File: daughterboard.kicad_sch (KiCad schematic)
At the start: 1 part, among them J1 Programming

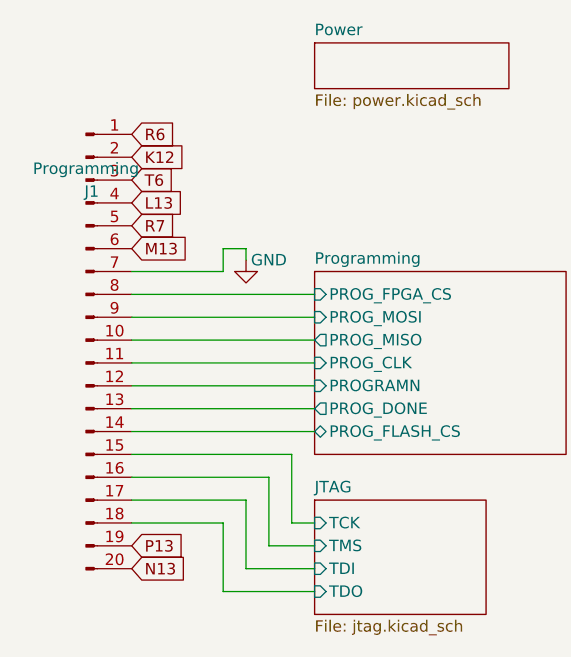
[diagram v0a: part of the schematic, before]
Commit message: Small routing tweaks, add breakout to schematic
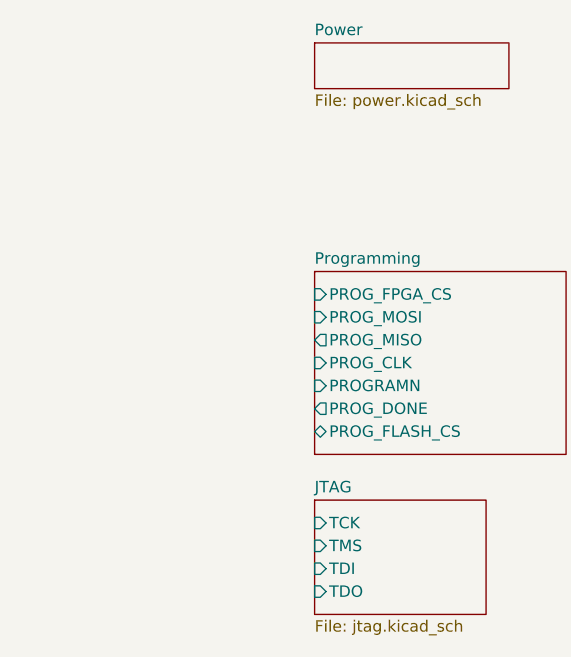
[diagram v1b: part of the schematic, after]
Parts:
- removed J1: Programming, Connector_PinHeader_2.54mm:PinHeader_2x10_P2.54mm_Vertical, symbol Connector:Conn_01x20_Pin
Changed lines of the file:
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@@
 (kicad_sch (version 20230121) (generator eeschema)
   (paper "A4")
-  (wire (pts (xy 123.19 104.14) (xy 118.11 104.14))
-    (stroke (width 0) (type default))
-  )
-  (wire (pts (xy 102.87 91.44) (xy 123.19 91.44))
-    (stroke (width 0) (type default))
-  )
-  (wire (pts (xy 113.03 71.12) (xy 113.03 73.66))
-    (stroke (width 0) (type default))
-  )
-  (wire (pts (xy 102.87 81.28) (xy 123.19 81.28))
-    (stroke (width 0) (type default))
-  )
-  (wire (pts (xy 102.87 101.6) (xy 113.03 101.6))
-    (stroke (width 0) (type default))
-  )
-  (wire (pts (xy 113.03 109.22) (xy 113.03 101.6))
-    (stroke (width 0) (type default))
-  )
-  (wire (pts (xy 120.65 93.98) (xy 120.65 101.6))
-    (stroke (width 0) (type default))
-  )
-  (wire (pts (xy 102.87 93.98) (xy 120.65 93.98))
-    (stroke (width 0) (type default))
-  )
-  (wire (pts (xy 123.19 106.68) (xy 115.57 106.68))
-    (stroke (width 0) (type default))
-  )
-  (wire (pts (xy 115.57 106.68) (xy 115.57 99.06))
-    (stroke (width 0) (type default))
-  )
-  (wire (pts (xy 115.57 71.12) (xy 113.03 71.12))
-    (stroke (width 0) (type default))
-  )
-  (wire (pts (xy 123.19 109.22) (xy 113.03 109.22))
-    (stroke (width 0) (type default))
-  )
-  (wire (pts (xy 102.87 96.52) (xy 118.11 96.52))
-    (stroke (width 0) (type default))
-  )
-  (wire (pts (xy 102.87 78.74) (xy 123.19 78.74))
-    (stroke (width 0) (type default))
-  )
-  (wire (pts (xy 102.87 88.9) (xy 123.19 88.9))
-    (stroke (width 0) (type default))
-  )
-  (wire (pts (xy 118.11 104.14) (xy 118.11 96.52))
-    (stroke (width 0) (type default))
-  )
-  (wire (pts (xy 115.57 72.39) (xy 115.57 71.12))
-    (stroke (width 0) (type default))
-  )
-  (wire (pts (xy 102.87 76.2) (xy 123.19 76.2))
-    (stroke (width 0) (type default))
-  )
-  (wire (pts (xy 102.87 83.82) (xy 123.19 83.82))
-    (stroke (width 0) (type default))
-  )
-  (wire (pts (xy 120.65 101.6) (xy 123.19 101.6))
-    (stroke (width 0) (type default))
-  )
-  (wire (pts (xy 102.87 99.06) (xy 115.57 99.06))
-    (stroke (width 0) (type default))
-  )
-  (wire (pts (xy 102.87 73.66) (xy 113.03 73.66))
-    (stroke (width 0) (type default))
-  )
-  (wire (pts (xy 102.87 86.36) (xy 123.19 86.36))
-    (stroke (width 0) (type default))
-  )
-  (global_label "T6" (shape input) (at 102.87 63.5 0) (fields_autoplaced)
-    (effects (font (size 1.27 1.27)) (justify left))
-    (property "Intersheetrefs" "${INTERSHEET_REFS}" (at 107.9529 63.5 0)
-      (effects (font (size 1.27 1.27)) (justify left) hide)
-    )
-  )
-  (global_label "K12" (shape input) (at 102.87 60.96 0) (fields_autoplaced)
-    (effects (font (size 1.27 1.27)) (justify left))
-    (property "Intersheetrefs" "${INTERSHEET_REFS}" (at 109.4648 60.96 0)
-      (effects (font (size 1.27 1.27)) (justify left) hide)
-    )
-  )
-  (global_label "N13" (shape input) (at 102.87 106.68 0) (fields_autoplaced)
-    (effects (font (size 1.27 1.27)) (justify left))
-    (property "Intersheetrefs" "${INTERSHEET_REFS}" (at 109.5253 106.68 0)
-      (effects (font (size 1.27 1.27)) (justify left) hide)
-    )
-  )
-  (global_label "M13" (shape input) (at 102.87 71.12 0) (fields_autoplaced)
-    (effects (font (size 1.27 1.27)) (justify left))
-    (property "Intersheetrefs" "${INTERSHEET_REFS}" (at 109.6462 71.12 0)
-      (effects (font (size 1.27 1.27)) (justify left) hide)
-    )
-  )
-  (global_label "L13" (shape input) (at 102.87 66.04 0) (fields_autoplaced)
-    (effects (font (size 1.27 1.27)) (justify left))
-    (property "Intersheetrefs" "${INTERSHEET_REFS}" (at 109.2229 66.04 0)
-      (effects (font (size 1.27 1.27)) (justify left) hide)
-    )
-  )
-  (global_label "R7" (shape input) (at 102.87 68.58 0) (fields_autoplaced)
-    (effects (font (size 1.27 1.27)) (justify left))
-    (property "Intersheetrefs" "${INTERSHEET_REFS}" (at 108.2553 68.58 0)
-      (effects (font (size 1.27 1.27)) (justify left) hide)
-    )
-  )
-  (global_label "P13" (shape input) (at 102.87 104.14 0) (fields_autoplaced)
-    (effects (font (size 1.27 1.27)) (justify left))
-    (property "Intersheetrefs" "${INTERSHEET_REFS}" (at 109.4648 104.14 0)
-      (effects (font (size 1.27 1.27)) (justify left) hide)
-    )
-  )
-  (global_label "R6" (shape input) (at 102.87 58.42 0) (fields_autoplaced)
-    (effects (font (size 1.27 1.27)) (justify left))
-    (property "Intersheetrefs" "${INTERSHEET_REFS}" (at 108.2553 58.42 0)
-      (effects (font (size 1.27 1.27)) (justify left) hide)
-    )
-  )
-  (symbol (lib_id "Connector:Conn_01x20_Pin") (at 97.79 81.28 0) (unit 1)
-    (in_bom yes) (on_board yes) (dnp no)
-    (property "Reference" "J1" (at 98.425 64.77 0)
-      (effects (font (size 1.27 1.27)))
-    )
-    (property "Value" "Programming" (at 97.79 62.23 0)
-      (effects (font (size 1.27 1.27)))
-    )
-    (property "Footprint" "Connector_PinHeader_2.54mm:PinHeader_2x10_P2.54mm_Vertical" (at 97.79 81.28 0)
-      (effects (font (size 1.27 1.27)) hide)
-    )
-    (property "Datasheet" "~" (at 97.79 81.28 0)
-      (effects (font (size 1.27 1.27)) hide)
-    )
-    (pin "1")
-    (pin "10")
-    (pin "11")
-    (pin "12")
-    (pin "13")
-    (pin "14")
-    (pin "15")
-    (pin "16")
-    (pin "17")
-    (pin "18")
-    (pin "19")
-    (pin "2")
-    (pin "20")
-    (pin "3")
-    (pin "4")
-    (pin "5")
-    (pin "6")
-    (pin "7")
-    (pin "8")
-    (pin "9")
-    (instances
-      (project "daughterboard"
-        (path "/dce8b7ce-114c-4680-a1bd-14f36a94838a"
-          (reference "J1") (unit 1)
-        )
-      )
-    )
-  )
-  (symbol (lib_id "power:GND") (at 115.57 72.39 0) (unit 1)
-    (in_bom yes) (on_board yes) (dnp no)
-    (property "Reference" "#PWR026" (at 115.57 78.74 0)
-      (effects (font (size 1.27 1.27)) hide)
-    )
-    (property "Value" "GND" (at 118.11 72.39 0)
-      (effects (font (size 1.27 1.27)))
-    )
-    (property "Footprint" "" (at 115.57 72.39 0)
-      (effects (font (size 1.27 1.27)) hide)
-    )
-    (property "Datasheet" "" (at 115.57 72.39 0)
-      (effects (font (size 1.27 1.27)) hide)
-    )
-    (pin "1")
-    (instances
-      (project "daughterboard"
-        (path "/dce8b7ce-114c-4680-a1bd-14f36a94838a"
-          (reference "#PWR026") (unit 1)
-        )
-      )
-    )
-  )
   (sheet (at 123.19 48.26) (size 21.59 5.08) (fields_autoplaced)
     (stroke (width 0.1524) (type solid))

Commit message: Route power
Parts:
- added J1: USB_C_Receptacle_USB2.0, Library:USB_C_GCT4105, symbol Connector:USB_C_Receptacle_USB2.0
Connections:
- new net 5VUSB: J1.A4 (VBUS), J1.A9 (VBUS), J1.B4 (VBUS), J1.B9 (VBUS)
- new net GND: J1.A1 (GND), J1.A12 (GND), J1.B1 (GND), J1.B12 (GND), J1.S1 (SHIELD)
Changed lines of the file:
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@@
 (kicad_sch (version 20230121) (generator eeschema)
   (paper "A4")
+  (junction (at 54.61 109.22) (diameter 0) (color 0 0 0 0)
+  )
+  (wire (pts (xy 54.61 109.22) (xy 58.42 109.22))
+    (stroke (width 0) (type default))
+  )
+  (wire (pts (xy 50.8 109.22) (xy 54.61 109.22))
+    (stroke (width 0) (type default))
+  )
+  (wire (pts (xy 58.42 109.22) (xy 58.42 106.68))
+    (stroke (width 0) (type default))
+  )
+  (wire (pts (xy 50.8 106.68) (xy 50.8 109.22))
+    (stroke (width 0) (type default))
+  )
+  (global_label "5VUSB" (shape input) (at 73.66 68.58 0) (fields_autoplaced)
+    (effects (font (size 1.27 1.27)) (justify left))
+    (property "Intersheetrefs" "${INTERSHEET_REFS}" (at 82.6739 68.58 0)
+      (effects (font (size 1.27 1.27)) (justify left) hide)
+    )
+  )
+  (symbol (lib_id "Connector:USB_C_Receptacle_USB2.0") (at 58.42 83.82 0) (unit 1)
+    (in_bom yes) (on_board yes) (dnp no) (fields_autoplaced)
+    (property "Reference" "J1" (at 58.42 62.23 0)
+      (effects (font (size 1.27 1.27)))
+    )
+    (property "Value" "USB_C_Receptacle_USB2.0" (at 58.42 64.77 0)
+      (effects (font (size 1.27 1.27)))
+    )
+    (property "Footprint" "Library:USB_C_GCT4105" (at 62.23 83.82 0)
+      (effects (font (size 1.27 1.27)) hide)
+    )
+    (property "Datasheet" "https://www.usb.org/sites/default/files/documents/usb_type-c.zip" (at 62.23 83.82 0)
+      (effects (font (size 1.27 1.27)) hide)
+    )
+    (pin "A1")
+    (pin "A12")
+    (pin "A4")
+    (pin "A5")
+    (pin "A6")
+    (pin "A7")
+    (pin "A8")
+    (pin "A9")
+    (pin "B1")
+    (pin "B12")
+    (pin "B4")
+    (pin "B5")
+    (pin "B6")
+    (pin "B7")
+    (pin "B8")
+    (pin "B9")
+    (pin "S1")
+    (instances
+      (project "daughterboard"
+        (path "/dce8b7ce-114c-4680-a1bd-14f36a94838a"
+          (reference "J1") (unit 1)
+        )
+      )
+    )
+  )
+  (symbol (lib_id "power:GND") (at 54.61 109.22 0) (unit 1)
+    (in_bom yes) (on_board yes) (dnp no) (fields_autoplaced)
+    (property "Reference" "#PWR026" (at 54.61 115.57 0)
+      (effects (font (size 1.27 1.27)) hide)
+    )
+    (property "Value" "GND" (at 54.61 114.3 0)
+      (effects (font (size 1.27 1.27)))
+    )
+    (property "Footprint" "" (at 54.61 109.22 0)
+      (effects (font (size 1.27 1.27)) hide)
+    )
+    (property "Datasheet" "" (at 54.61 109.22 0)
+      (effects (font (size 1.27 1.27)) hide)
+    )
+    (pin "1")
+    (instances
+      (project "daughterboard"
+        (path "/dce8b7ce-114c-4680-a1bd-14f36a94838a/233da297-15ca-4163-a51b-09f27dce3135"
+          (reference "#PWR026") (unit 1)
+        )
+        (path "/dce8b7ce-114c-4680-a1bd-14f36a94838a"
+          (reference "#PWR032") (unit 1)
+        )
+      )
+    )
+  )
   (sheet (at 123.19 48.26) (size 21.59 5.08) (fields_autoplaced)
     (stroke (width 0.1524) (type solid))

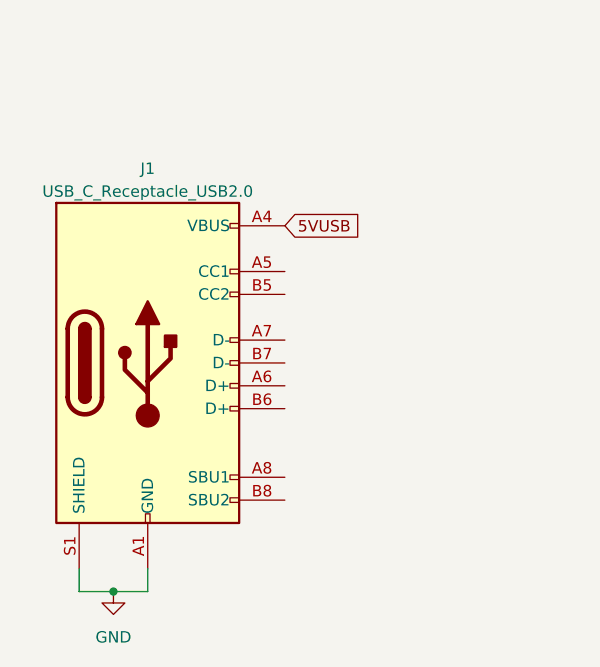
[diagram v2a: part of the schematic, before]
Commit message: Route power, FTDI chip
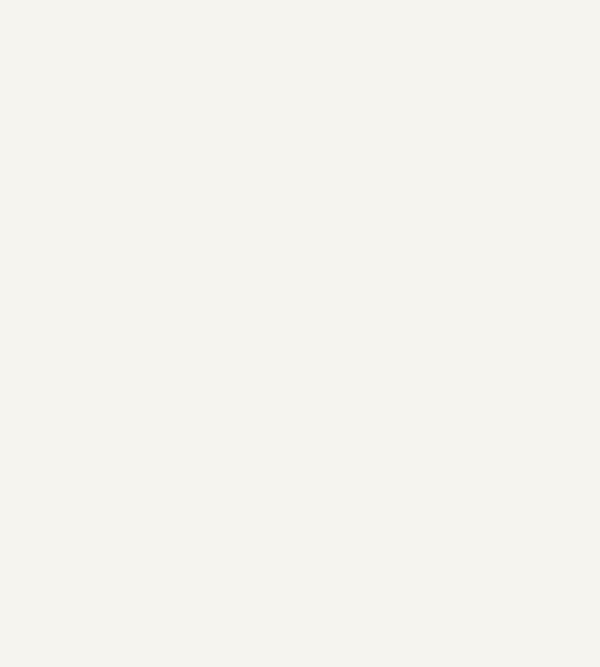
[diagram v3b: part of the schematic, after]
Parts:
- removed J1: USB_C_Receptacle_USB2.0, Library:USB_C_GCT4105, symbol Connector:USB_C_Receptacle_USB2.0
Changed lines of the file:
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@@
 (kicad_sch (version 20230121) (generator eeschema)
   (paper "A4")
-  (junction (at 54.61 109.22) (diameter 0) (color 0 0 0 0)
-  )
-  (wire (pts (xy 54.61 109.22) (xy 58.42 109.22))
-    (stroke (width 0) (type default))
-  )
-  (wire (pts (xy 50.8 109.22) (xy 54.61 109.22))
-    (stroke (width 0) (type default))
-  )
-  (wire (pts (xy 58.42 109.22) (xy 58.42 106.68))
-    (stroke (width 0) (type default))
-  )
-  (wire (pts (xy 50.8 106.68) (xy 50.8 109.22))
-    (stroke (width 0) (type default))
-  )
-  (global_label "5VUSB" (shape input) (at 73.66 68.58 0) (fields_autoplaced)
-    (effects (font (size 1.27 1.27)) (justify left))
-    (property "Intersheetrefs" "${INTERSHEET_REFS}" (at 82.6739 68.58 0)
-      (effects (font (size 1.27 1.27)) (justify left) hide)
-    )
-  )
-  (symbol (lib_id "Connector:USB_C_Receptacle_USB2.0") (at 58.42 83.82 0) (unit 1)
-    (in_bom yes) (on_board yes) (dnp no) (fields_autoplaced)
-    (property "Reference" "J1" (at 58.42 62.23 0)
-      (effects (font (size 1.27 1.27)))
-    )
-    (property "Value" "USB_C_Receptacle_USB2.0" (at 58.42 64.77 0)
-      (effects (font (size 1.27 1.27)))
-    )
-    (property "Footprint" "Library:USB_C_GCT4105" (at 62.23 83.82 0)
-      (effects (font (size 1.27 1.27)) hide)
-    )
-    (property "Datasheet" "https://www.usb.org/sites/default/files/documents/usb_type-c.zip" (at 62.23 83.82 0)
-      (effects (font (size 1.27 1.27)) hide)
-    )
-    (pin "A1")
-    (pin "A12")
-    (pin "A4")
-    (pin "A5")
-    (pin "A6")
-    (pin "A7")
-    (pin "A8")
-    (pin "A9")
-    (pin "B1")
-    (pin "B12")
-    (pin "B4")
-    (pin "B5")
-    (pin "B6")
-    (pin "B7")
-    (pin "B8")
-    (pin "B9")
-    (pin "S1")
-    (instances
-      (project "daughterboard"
-        (path "/dce8b7ce-114c-4680-a1bd-14f36a94838a"
-          (reference "J1") (unit 1)
-        )
-      )
-    )
-  )
-  (symbol (lib_id "power:GND") (at 54.61 109.22 0) (unit 1)
-    (in_bom yes) (on_board yes) (dnp no) (fields_autoplaced)
-    (property "Reference" "#PWR026" (at 54.61 115.57 0)
-      (effects (font (size 1.27 1.27)) hide)
-    )
-    (property "Value" "GND" (at 54.61 114.3 0)
-      (effects (font (size 1.27 1.27)))
-    )
-    (property "Footprint" "" (at 54.61 109.22 0)
-      (effects (font (size 1.27 1.27)) hide)
-    )
-    (property "Datasheet" "" (at 54.61 109.22 0)
-      (effects (font (size 1.27 1.27)) hide)
-    )
-    (pin "1")
-    (instances
-      (project "daughterboard"
-        (path "/dce8b7ce-114c-4680-a1bd-14f36a94838a/233da297-15ca-4163-a51b-09f27dce3135"
-          (reference "#PWR026") (unit 1)
-        )
-        (path "/dce8b7ce-114c-4680-a1bd-14f36a94838a"
-          (reference "#PWR032") (unit 1)
-        )
-      )
-    )
-  )
   (sheet (at 123.19 48.26) (size 21.59 5.08) (fields_autoplaced)
     (stroke (width 0.1524) (type solid))
